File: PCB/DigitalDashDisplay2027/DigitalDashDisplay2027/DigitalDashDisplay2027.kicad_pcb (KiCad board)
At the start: 2 copper layers, 100 x 56.3 mm, 13 parts, among them IC2 LMR51430YDDCR, U1 Teensy4.0

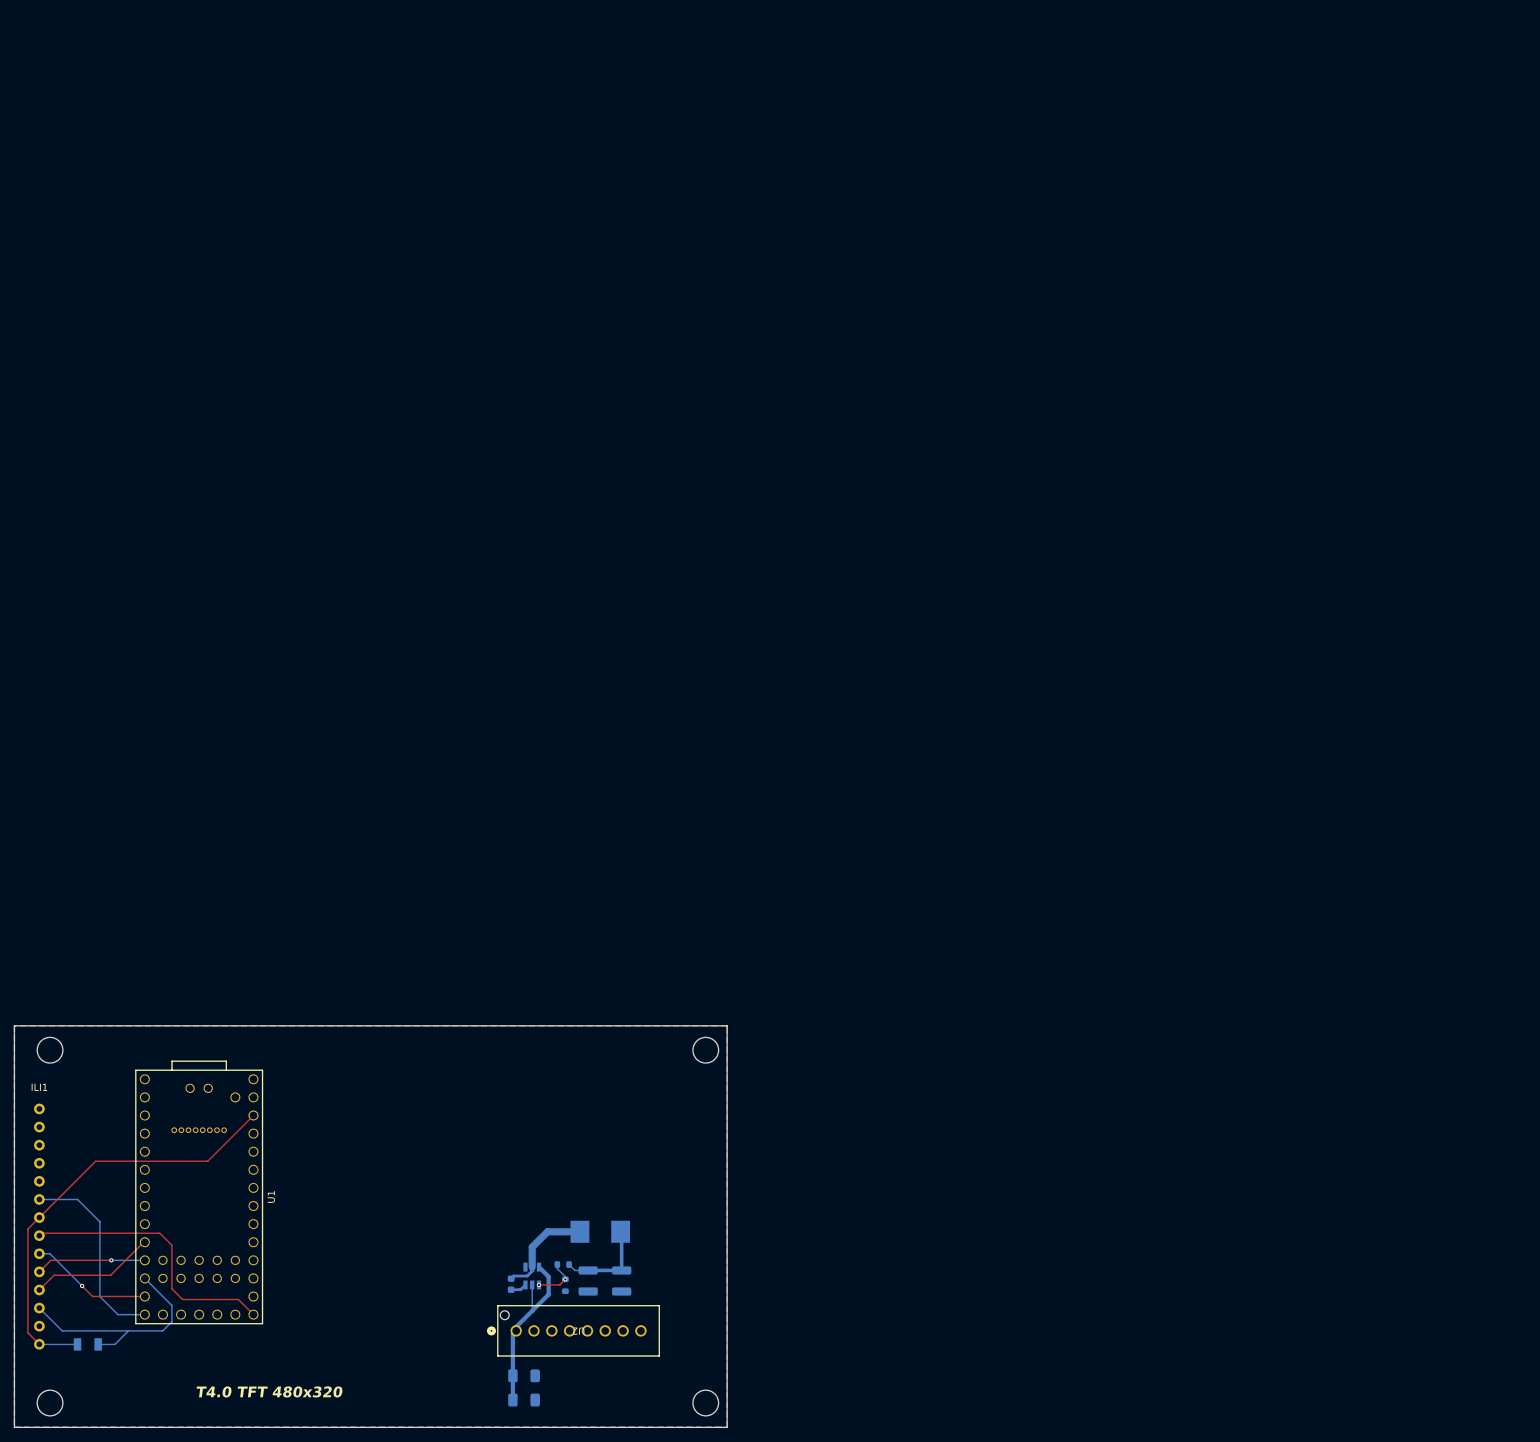
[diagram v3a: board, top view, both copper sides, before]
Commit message: V1.0 of dashboard, plus minor changes to DAQ board
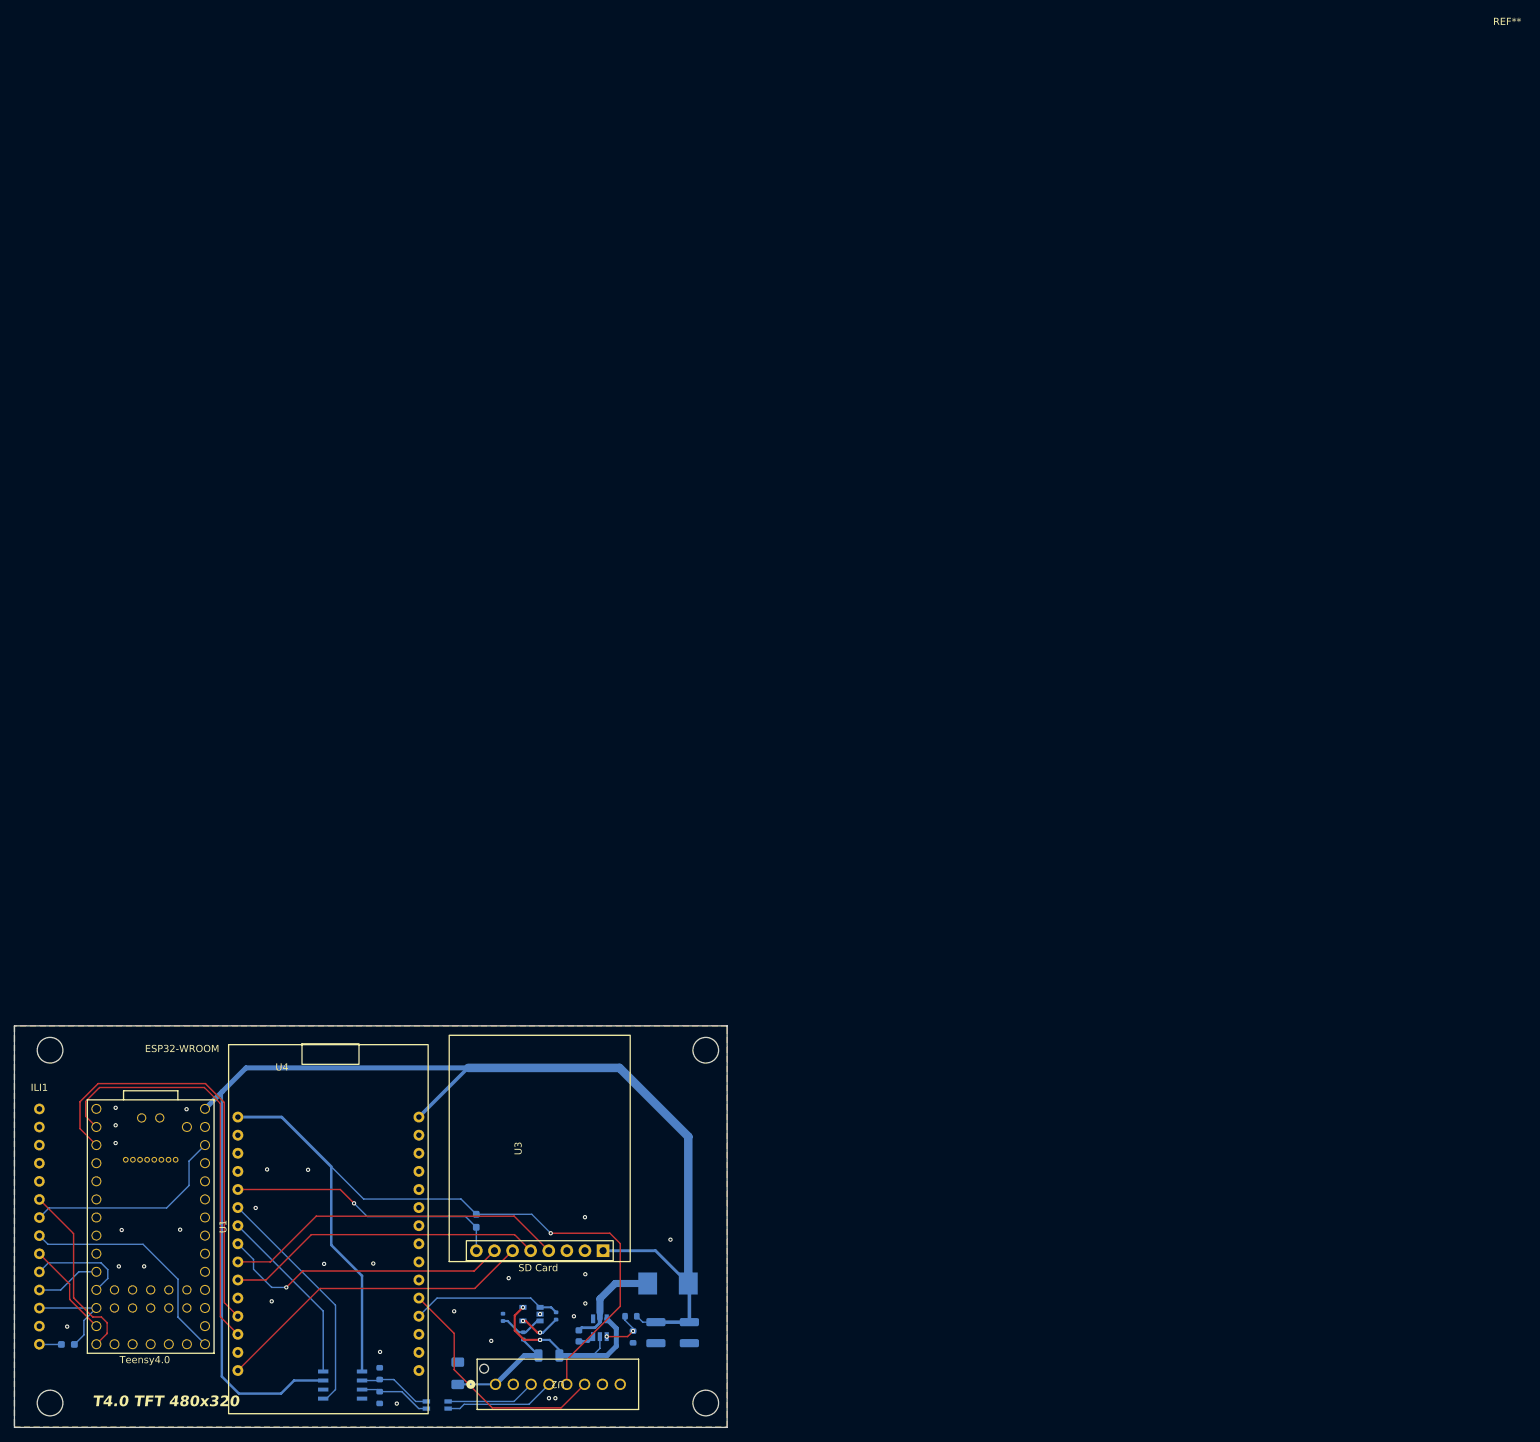
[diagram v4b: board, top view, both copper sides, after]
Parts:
- removed C5: C3216X5R1E476M160AC, Capacitor_SMD:C_1206_3216Metric_Pad1.33x1.80mm_HandSolder
- added R10: 10k, Resistor_SMD:R_0603_1608Metric_Pad0.98x0.95mm_HandSolder, B.Cu at (175.8, 94.8)
- added R11: CSR1206FT50L0, Resistor_SMD:R_1206_3216Metric, B.Cu at (186.0, 113.8)
- added R3: 60, Resistor_SMD:R_0603_1608Metric, B.Cu at (162.2, 119.7)
- added R4: 60, Resistor_SMD:R_0603_1608Metric, B.Cu at (162.2, 116.3)
- added R5: 56.2k, Resistor_SMD:R_0402_1005Metric, B.Cu at (179.6, 108.4)
- added R6: 22.1k, Resistor_SMD:R_0402_1005Metric, B.Cu at (187.0, 108.2)
- added R7: 100k, Resistor_SMD:R_0402_1005Metric, B.Cu at (184.8, 111.0)
- added R9: 10k, Resistor_SMD:R_0603_1608Metric_Pad0.98x0.95mm_HandSolder, B.Cu at (118.5, 112.2)
- added REF**: Adafruit 254, CFR-Footprint-Library:Adafruit 254, F.Cu at (314.4, -66.6)
- added T1: ~, CFR-Footprint-Library:AC1210-110-C, B.Cu at (168.8, 121.2)
- added T2: ~, CFR-Footprint-Library:NCS2005SN1T1G, B.Cu at (184.8, 108.9)
- added U3: ~, CFR-Footprint-Library:Adafruit 254, F.Cu at (175.8, 99.1)
- added U4: ~, CFR-Footprint-Library:ESP32, F.Cu at (142.3, 80.3)
- added U5: TCAN1051VDRQ1, CFR-Footprint-Library:D8_TEX, B.Cu at (157.1, 117.9)
- R8: value 1206W4J0103T5E -> 100k; footprint SamacSys_Parts:RESC3116X65N -> Resistor_SMD:R_0402_1005Metric
- moved R8 61.1 mm to (182.4, 111.0), turned to 90 degrees
- moved C1 12.0 mm to (190.2, 111.0)
- moved C3 12.0 mm to (201.0, 110.5)
- moved C4 12.0 mm to (205.7, 110.5)
- moved IC2 12.0 mm to (193.2, 109.8)
- moved L1 12.0 mm to (202.7, 103.7)
- moved R1 12.0 mm to (197.5, 108.2)
- moved R2 12.0 mm to (197.8, 111.2)
- moved C2 10.0 mm to (173.2, 116.2), turned to -90 degrees
- moved U2 8.04 mm to (178.5, 117.8)
- moved U1 7.97 mm to (130.1, 95.7)
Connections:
- net /Clock renamed /TFT_Clk
- net /MISO renamed /TFT_MISO
- net /MOSI renamed /TFT_MOSI
- net GNDREF renamed /GND
- C2 pad 2: +BATT -> /CurrentSense
- IC2 pad 3: +BATT -> /+12V
- IC2 pad 5: +BATT -> /+12V
- ILI1 pad 12: /Control Signal -> /TFT_CS
- ILI1 pad 14: +3.3V -> /3V3_Teen
- ILI1 pad 7: +3.3V -> /3V3_Teen
- R8 pad 1: +3.3V -> /CurrentSense
- R8 pad 2: /Control Signal -> Net-(T2-+)
- U1 pad 12: /Control Signal -> /TFT_CS
- U1 pad 2: unconnected-(U1-0_RX1_CRX2_CS1-Pad2) -> /TIn_EOut
- U1 pad 29: /CTX -> unconnected-(U1-22_A8_CTX1-Pad29)
- U1 pad 3: unconnected-(U1-1_TX1_CTX2_MISO1-Pad3) -> /TOut_EIn
- U1 pad 30: /CRX -> unconnected-(U1-23_A9_CRX1_MCLK1-Pad30)
- U1 pad 31: +3.3V -> /3V3_Teen
- U2 pad 1: +BATT -> /CurrentSense
- U2 pad 3: /CanHi -> /CAN Lo
- U2 pad 4: /CanLo -> /CAN Hi
- U2 pad 5: unconnected-(U2-1-Pad5) -> /3V3_ESP
- U2 pad 6: unconnected-(U2-2-Pad6) -> /DAQ_Button
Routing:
- net +5V: track 13.2 -> 188.3 mm
- net /3V3_ESP: track 0.00 -> 114.4 mm, vias 0 -> 1
- net +3.3V: track 60.5 -> 0.00 mm
- net /TOut_EIn: track 0.00 -> 60.2 mm
- net /TIn_EOut: track 0.00 -> 58.2 mm
- net /SD_CLK: track 0.00 -> 48.3 mm
- net /SD_MOSI: track 0.00 -> 45.5 mm
- net /SD_MISO: track 0.00 -> 44.6 mm
- net /SD_CS: track 0.00 -> 41.5 mm, vias 0 -> 1
- net /SD_CD: track 0.00 -> 38.9 mm, vias 0 -> 1
- net /DAQ_Button: track 0.00 -> 34.0 mm
- net /CANRx: track 0.00 -> 33.5 mm
- net /Control Signal: track 33.1 -> 0.00 mm
- net /3V3_Teen: track 0.00 -> 32.6 mm
- net /+12V: track 0.00 -> 27.9 mm, vias 0 -> 2
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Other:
- board text added: "CAN"
- board text added: "Current Sense"
- board text added: "ESP32-WROOM"
- board text added: "SD Card"
- board text added: "Teensy4.0"

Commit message: Finalized A-A filters, finishing touches on DAQ and Dash boards
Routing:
- net /3V3_Teen: track 32.6 -> 52.1 mm
- net /GND: vias 28 -> 38
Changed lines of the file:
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@@
+	)
+	(via
+		(at 209.05 114.35)
+		(size 0.6)
+		(drill 0.3)
+		(layers "F.Cu" "B.Cu")
+		(free yes)
+		(net "/GND")
+	)
+	(via
+		(at 122.15 121.4)
+		(size 0.6)
+		(drill 0.3)
+		(layers "F.Cu" "B.Cu")
+		(free yes)
+		(net "/GND")
 	)
 	(via
@@
 	)
 	(via
+		(at 183.05 115.7)
+		(size 0.6)
+		(drill 0.3)
+		(layers "F.Cu" "B.Cu")
+		(free yes)
+		(net "/GND")
+	)
+	(via
 		(at 125.65 101.25)
 		(size 0.6)
@@
 	)
 	(via
+		(at 121.95 69.45)
+		(size 0.6)
+		(drill 0.3)
+		(layers "F.Cu" "B.Cu")
+		(free yes)
+		(net "/GND")
+	)
+	(via
 		(at 172.7 107.55)
 		(size 0.6)
@@
 	)
 	(via
+		(at 186 115.7)
+		(size 0.6)
+		(drill 0.3)
+		(layers "F.Cu" "B.Cu")
+		(free yes)
+		(net "/GND")
+	)
+	(via
 		(at 146.45 87.65)
 		(size 0.6)
@@
 	)
 	(via
+		(at 179.75 119.2)
+		(size 0.6)
+		(drill 0.3)
+		(layers "F.Cu" "B.Cu")
+		(free yes)
+		(net "/GND")
+	)
+	(via
 		(at 129.2 101.25)
 		(size 0.6)
@@
 	)
 	(via
+		(at 201.75 122.25)
+		(size 0.6)
+		(drill 0.3)
+		(layers "F.Cu" "B.Cu")
+		(free yes)
+		(net "/GND")
+	)
+	(via
 		(at 125.2 81.45)
 		(size 0.6)
@@
 	)
 	(via
+		(at 208.9 76.4)
+		(size 0.6)
+		(drill 0.3)
+		(layers "F.Cu" "B.Cu")
+		(free yes)
+		(net "/GND")
+	)
+	(via
+		(at 113 114.85)
+		(size 0.6)
+		(drill 0.3)
+		(layers "F.Cu" "B.Cu")
+		(free yes)
+		(net "/GND")
+	)
+	(via
 		(at 162.3 113.25)
+		(size 0.6)
+		(drill 0.3)
+		(layers "F.Cu" "B.Cu")
+		(free yes)
+		(net "/GND")
+	)
+	(via
+		(at 202 69.5)
 		(size 0.6)
 		(drill 0.3)
@@
 	)
 	(segment
+		(start 112.4 110.08)
+		(end 112.4 96.5)
+		(width 0.2)
+		(layer "F.Cu")
+		(net "/3V3_Teen")
+	)
+	(segment
+		(start 112.4 96.5)
+		(end 114.5 94.4)
+		(width 0.2)
+		(layer "F.Cu")
+		(net "/3V3_Teen")
+	)
+	(segment
+		(start 114.5 112.18)
+		(end 112.4 110.08)
+		(width 0.2)
+		(layer "F.Cu")
+		(net "/3V3_Teen")
+	)
+	(segment

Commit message: Finishing touches on dashboard, finished PDM with stitched vias, continued work on dashboard teensy code
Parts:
- added R12: 10k, Resistor_SMD:R_0603_1608Metric_Pad0.98x0.95mm_HandSolder, B.Cu at (171.4, 110.3)
- C2: value C3216X5R1E476M160AC -> C3216X5R1E476MTJ00E
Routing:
- net /GND: vias 38 -> 40
- net /DAQ_Button: vias 0 -> 1

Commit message: Fixed dashboard sd card reader footprint, updated 2027 dash code with rpm numbers
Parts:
- U3: moved to B.Cu
- moved U3 17.8 mm to (193.6, 99.0)
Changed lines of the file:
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@@
 	(footprint "CFR-Footprint-Library:Adafruit 254"
 		(layer "F.Cu")
-		(at 175.81 99.051 90)
-		(property "Reference" "U3"
-			(at 14.351 5.89 90)
-			(unlocked yes)
-			(layer "F.SilkS")
-			(effects
-				(font
-					(size 1 1)
-					(thickness 0.1)
-				)
-			)
-		)
-		(property "Value" "~"
-			(at 14.351 7.39 90)
-			(unlocked yes)
-			(layer "F.Fab")
-			(effects
-				(font
-					(size 1 1)
-					(thickness 0.15)
-				)
-			)
-		)
-		(property "Datasheet" ""
-			(at 0 0 90)
-			(unlocked yes)
-			(layer "F.Fab")
-			(hide yes)
-			(effects
-				(font
-					(size 1 1)
-					(thickness 0.15)
-				)
-			)
-		)
-		(property "Description" ""
-			(at 0 0 90)
-			(unlocked yes)
-			(layer "F.Fab")
-			(hide yes)
-			(effects
-				(font
-					(size 1 1)
-					(thickness 0.15)
-				)
-			)
-		)
-		(sheetname "/")
-		(sheetfile "DigitalDashDisplay2027.kicad_sch")
-		(units
-			(unit
-				(name "A")
-				(pins "8" "7" "6" "5" "4" "3" "2" "1")
-			)
-		)
-		(attr smd dnp)
-		(duplicate_pad_numbers_are_jumpers no)
-		(fp_rect
-			(start -1.524 -3.81)
-			(end 30.226 21.59)
-			(stroke
-				(width 0.1)
-				(type solid)
-			)
-			(fill no)
-			(layer "F.SilkS")
-		)
-		(fp_rect
-			(start -1.4 -1.4)
-			(end 1.4 19.2)
-			(stroke
-				(width 0.1)
-				(type default)
-			)
-			(fill no)
-			(layer "F.SilkS")
-		)
-		(fp_text user "${REFERENCE}"
-			(at 14.351 8.89 90)
-			(unlocked yes)
-			(layer "F.Fab")
-			(effects
-				(font
-					(size 1 1)
-					(thickness 0.15)
-				)
-			)
-		)
-		(pad "1" thru_hole rect
-			(at 0 17.78 180)
-			(size 1.778 1.778)
-			(drill 1)
-			(layers "*.Cu" "*.Mask")
-			(remove_unused_layers no)
-			(net "+5V")
-			(pinfunction "5V_1")
-			(pintype "input")
-			(solder_mask_margin 0.0508)
-			(thermal_bridge_angle 0)
-		)
-		(pad "2" thru_hole circle
-			(at 0 15.24 180)
-			(size 1.778 1.778)
-			(drill 1)
-			(layers "*.Cu" "*.Mask")
-			(remove_unused_layers no)
-			(net "unconnected-(U3-3V3-Pad2)")
-			(pinfunction "3V3_2")
-			(pintype "input+no_connect")
-			(solder_mask_margin 0.0508)
-			(thermal_bridge_angle 0)
-		)
-		(pad "3" thru_hole circle
-			(at 0 12.7 180)
-			(size 1.778 1.778)
-			(drill 1)
-			(layers "*.Cu" "*.Mask")
-			(remove_unused_layers no)
-			(net "/GND")
-			(pinfunction "GND_3")
-			(pintype "input")
-			(solder_mask_margin 0.0508)
-			(thermal_bridge_angle 0)
-		)
-		(pad "4" thru_hole circle
-			(at 0 10.16 180)
-			(size 1.778 1.778)
-			(drill 1)
-			(layers "*.Cu" "*.Mask")
-			(remove_unused_layers no)
-			(net "/SD_CLK")
-			(pinfunction "CLK_4")
-			(pintype "input")
-			(solder_mask_margin 0.0508)
-			(thermal_bridge_angle 0)
-		)
-		(pad "5" thru_hole circle
-			(at 0 7.62 180)
-			(size 1.778 1.778)
-			(drill 1)
-			(layers "*.Cu" "*.Mask")
-			(remove_unused_layers no)
-			(net "/SD_MISO")
-			(pinfunction "D0_5")
-			(pintype "output")
-			(solder_mask_margin 0.0508)
-			(thermal_bridge_angle 0)
-		)
-		(pad "6" thru_hole circle
-			(at 0 5.08 180)
-			(size 1.778 1.778)
-			(drill 1)
-			(layers "*.Cu" "*.Mask")
-			(remove_unused_layers no)
-			(net "/SD_MOSI")
-			(pinfunction "DI_6")
-			(pintype "input")
-			(solder_mask_margin 0.0508)
-			(thermal_bridge_angle 0)
-		)
-		(pad "7" thru_hole circle
-			(at 0 2.54 180)
-			(size 1.778 1.778)
-			(drill 1)
-			(layers "*.Cu" "*.Mask")
-			(remove_unused_layers no)
-			(net "/SD_CS")
-			(pinfunction "CS_7")
-			(pintype "input")
-			(solder_mask_margin 0.0508)
-			(thermal_bridge_angle 0)
-		)
-		(pad "8" thru_hole circle
-			(at 0 0 180)
-			(size 1.778 1.778)
-			(drill 1)
-			(layers "*.Cu" "*.Mask")
-			(remove_unused_layers no)
-			(net "/SD_CD")
-			(pinfunction "CD_8")
-			(pintype "input")
-			(solder_mask_margin 0.0508)
-			(thermal_bridge_angle 0)
-		)
-		(embedded_fonts no)
-	)
-	(footprint "CFR-Footprint-Library:Adafruit 254"
-		(layer "F.Cu")
 		(at 314.45 -66.6)
 		(property "Reference" "REF**"
@@
 		)
 	)
+	(footprint "CFR-Footprint-Library:Adafruit 254"
+		(layer "B.Cu")
+		(at 193.58 99.05 90)
+		(property "Reference" "U3"
+			(at 14.351 -5.89 270)
+			(unlocked yes)
+			(layer "B.SilkS")
+			(effects
+				(font
+					(size 1 1)
+					(thickness 0.1)
+				)
+				(justify mirror)
+			)
+		)
+		(property "Value" "~"
+			(at 14.351 -7.39 270)
+			(unlocked yes)
+			(layer "B.Fab")
+			(effects
+				(font
+					(size 1 1)
+					(thickness 0.15)
+				)
+				(justify mirror)
+			)
+		)
+		(property "Datasheet" ""
+			(at 0 0 270)
+			(unlocked yes)
+			(layer "B.Fab")
+			(hide yes)
+			(effects
+				(font
+					(size 1 1)
+					(thickness 0.15)
+				)
+				(justify mirror)
+			)
+		)
+		(property "Description" ""
+			(at 0 0 270)
+			(unlocked yes)
+			(layer "B.Fab")
+			(hide yes)
+			(effects
+				(font
+					(size 1 1)
+					(thickness 0.15)
+				)
+				(justify mirror)
+			)
+		)
+		(sheetname "/")
+		(sheetfile "DigitalDashDisplay2027.kicad_sch")
+		(attr smd dnp)
+		(duplicate_pad_numbers_are_jumpers no)
+		(fp_rect
+			(start -1.4 1.4)
+			(end 1.4 -19.2)
+			(stroke
+				(width 0.1)
+				(type default)
+			)
+			(fill no)
+			(layer "B.SilkS")
+		)
+		(fp_rect
+			(start -1.524 3.81)
+			(end 30.226 -21.59)
+			(stroke
+				(width 0.1)
+				(type solid)
+			)
+			(fill no)
+			(layer "B.SilkS")
+		)
+		(fp_text user "${REFERENCE}"
+			(at 14.351 -8.89 270)
+			(unlocked yes)
+			(layer "B.Fab")
+			(effects
+				(font
+					(size 1 1)
+					(thickness 0.15)
+				)
+				(justify mirror)
+			)
+		)
+		(pad "1" thru_hole rect
+			(at 0 0)
+			(size 1.778 1.778)
+			(drill 1)
+			(layers "*.Cu" "*.Mask")
+			(remove_unused_layers no)
+			(net "+5V")
+			(pinfunction "5V_1")
+			(pintype "input")
+			(solder_mask_margin 0.0508)
+			(thermal_bridge_angle 0)
+		)
+		(pad "2" thru_hole circle
+			(at 0 -2.54)
+			(size 1.778 1.778)
+			(drill 1)
+			(layers "*.Cu" "*.Mask")
+			(remove_unused_layers no)
+			(net "unconnected-(U3-3V3-Pad2)")
+			(pinfunction "3V3_2")
+			(pintype "input+no_connect")
+			(solder_mask_margin 0.0508)
+			(thermal_bridge_angle 0)
+		)
+		(pad "3" thru_hole circle
+			(at 0 -5.08)
+			(size 1.778 1.778)
+			(drill 1)
+			(layers "*.Cu" "*.Mask")
+			(remove_unused_layers no)
+			(net "/GND")
+			(pinfunction "GND_3")
+			(pintype "input")
+			(solder_mask_margin 0.0508)
+			(thermal_bridge_angle 0)
+		)
+		(pad "4" thru_hole circle
+			(at 0 -7.62)
+			(size 1.778 1.778)
+			(drill 1)
+			(layers "*.Cu" "*.Mask")
+			(remove_unused_layers no)
+			(net "/SD_CLK")
+			(pinfunction "CLK_4")
+			(pintype "input")
+			(solder_mask_margin 0.0508)
+			(thermal_bridge_angle 0)
+		)
+		(pad "5" thru_hole circle
+			(at 0 -10.16)
+			(size 1.778 1.778)
+			(drill 1)
+			(layers "*.Cu" "*.Mask")
+			(remove_unused_layers no)
+			(net "/SD_MISO")
+			(pinfunction "D0_5")
+			(pintype "output")
+			(solder_mask_margin 0.0508)
+			(thermal_bridge_angle 0)
+		)
+		(pad "6" thru_hole circle
+			(at 0 -12.7)
+			(size 1.778 1.778)
+			(drill 1)
+			(layers "*.Cu" "*.Mask")
+			(remove_unused_layers no)
+			(net "/SD_MOSI")
+			(pinfunction "DI_6")
+			(pintype "input")
+			(solder_mask_margin 0.0508)
+			(thermal_bridge_angle 0)
+		)
+		(pad "7" thru_hole circle
+			(at 0 -15.24)
+			(size 1.778 1.778)
+			(drill 1)
+			(layers "*.Cu" "*.Mask")
+			(remove_unused_layers no)
+			(net "/SD_CS")
+			(pinfunction "CS_7")
+			(pintype "input")
+			(solder_mask_margin 0.0508)
+			(thermal_bridge_angle 0)
+		)
+		(pad "8" thru_hole circle
+			(at 0 -17.78)
+			(size 1.778 1.778)
+			(drill 1)
+			(layers "*.Cu" "*.Mask")
+			(remove_unused_layers no)
+			(net "/SD_CD")
+			(pinfunction "CD_8")
+			(pintype "input")
+			(solder_mask_margin 0.0508)
+			(thermal_bridge_angle 0)
+		)
+		(embedded_fonts no)
+	)
 	(footprint "Capacitor_SMD:C_1206_3216Metric_Pad1.33x1.80mm_HandSolder"
